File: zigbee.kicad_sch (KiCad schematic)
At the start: 13 parts, among them J2001 TC2050, J2003 SMA-KWE901, U2001 CC2652PSIP

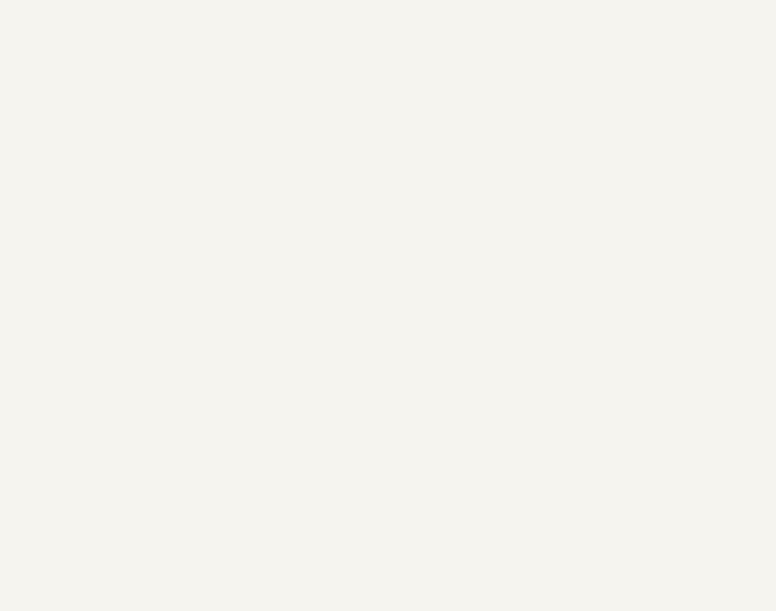
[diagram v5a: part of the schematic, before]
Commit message: Added header pins for UART5
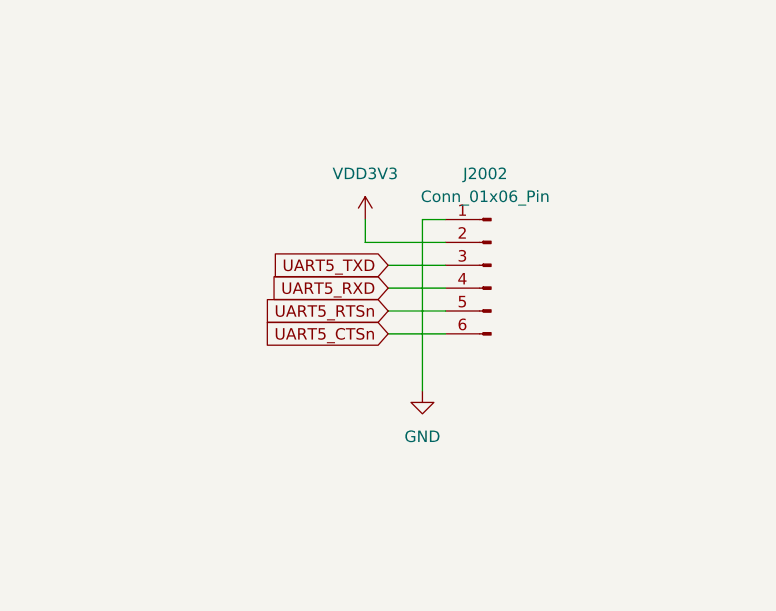
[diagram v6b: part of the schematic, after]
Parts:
- added J2002: Conn_01x06_Pin, Connector_PinHeader_2.54mm:PinHeader_1x06_P2.54mm_Vertical, symbol Connector:Conn_01x06_Pin
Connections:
- net GND: now also J2002.1 (Pin_1)
- new net UART5_CTSn: J2002.6 (Pin_6)
- new net UART5_RTSn: J2002.5 (Pin_5)
- new net UART5_RXD: J2002.4 (Pin_4)
- new net UART5_TXD: J2002.3 (Pin_3)
- new net VDD3V3: J2002.2 (Pin_2)

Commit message: Added almost all passive component footprints
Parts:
- C2001, C2002: footprint (none) -> Capacitor_SMD:C_0201_0603Metric
- D2001, D2002, D2003: footprint (none) -> Diode_SMD:D_SOD-523
- FB2001, R2001, R2002, R2003, R2004: footprint (none) -> Resistor_SMD:R_0402_1005Metric
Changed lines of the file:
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@@
 			)
 		)
-		(property "Footprint" ""
+		(property "Footprint" "Diode_SMD:D_SOD-523"
 			(at 182.88 184.15 0)
 			(effects
@@
 			)
 		)
-		(property "Footprint" ""
+		(property "Footprint" "Diode_SMD:D_SOD-523"
 			(at 182.88 189.23 0)
 			(effects
@@
 			)
 		)
-		(property "Footprint" ""
+		(property "Footprint" "Capacitor_SMD:C_0201_0603Metric"
 			(at 160.02 100.6348 0)
 			(effects
@@
 			)
 		)
-		(property "Footprint" ""
+		(property "Footprint" "Resistor_SMD:R_0402_1005Metric"
 			(at 207.01 80.518 90)
 			(effects
@@
 			)
 		)
-		(property "Footprint" ""
+		(property "Footprint" "Resistor_SMD:R_0402_1005Metric"
 			(at 157.48 156.718 90)
 			(effects
@@
 			)
 		)
-		(property "Footprint" ""
+		(property "Footprint" "Capacitor_SMD:C_0201_0603Metric"
 			(at 89.8652 104.14 0)
 			(effects
@@
 			)
 		)
-		(property "Footprint" ""
+		(property "Footprint" "Resistor_SMD:R_0402_1005Metric"
 			(at 157.48 141.478 90)
 			(effects
@@
 			)
 		)
-		(property "Footprint" ""
+		(property "Footprint" "Resistor_SMD:R_0402_1005Metric"
 			(at 157.48 154.178 90)
 			(effects
@@
 			)
 		)
-		(property "Footprint" ""
+		(property "Footprint" "Resistor_SMD:R_0402_1005Metric"
 			(at 157.48 138.938 90)
 			(effects
@@
 			)
 		)
-		(property "Footprint" ""
+		(property "Footprint" "Diode_SMD:D_SOD-523"
 			(at 182.88 194.31 0)
 			(effects

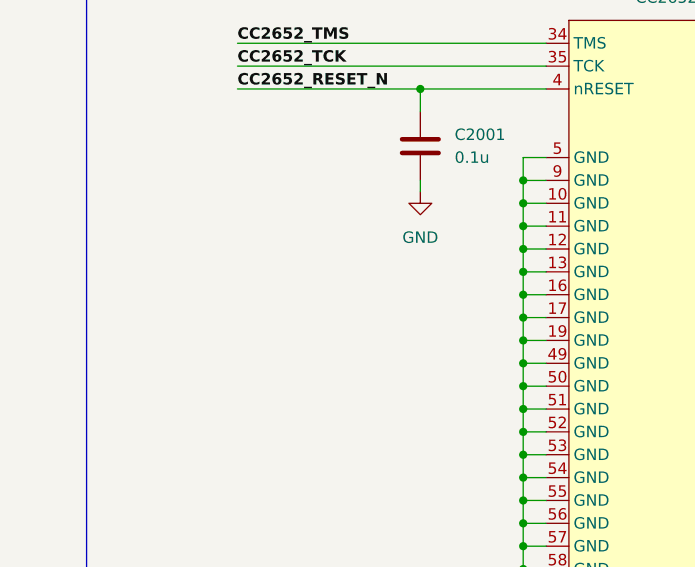
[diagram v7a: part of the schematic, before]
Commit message: Cleaned up schematic
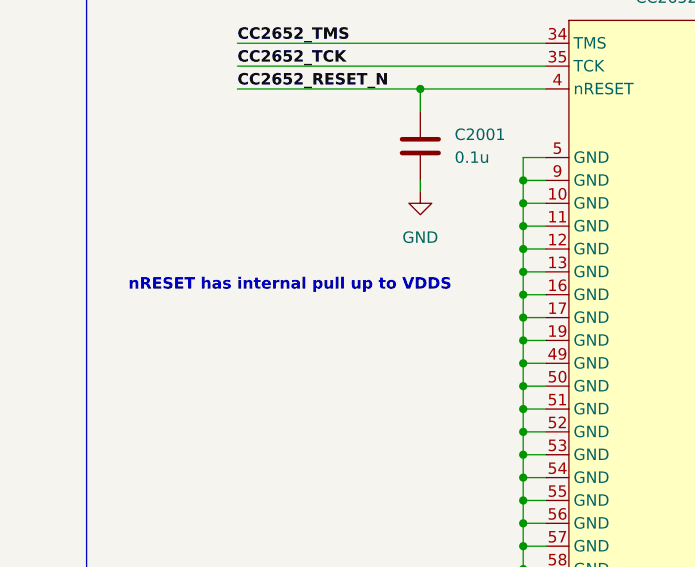
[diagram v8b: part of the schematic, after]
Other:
- note added: "nRESET has internal pull up to VDDS"
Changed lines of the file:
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@@
+		)
+	)
+	(text "nRESET has internal pull up to VDDS"
+		(exclude_from_sim no)
+		(at 74.422 115.824 0)
+		(effects
+			(font
+				(size 1.27 1.27)
+				(thickness 0.254)
+				(bold yes)
+			)
 		)
 	)
